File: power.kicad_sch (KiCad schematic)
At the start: 24 parts, among them U1 AP63203WU, U4 XL1509-12, U6 XL1509-12

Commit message: ESC Update with Specifications
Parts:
- C1: value 10uF -> 10u
- C12, C5: value 470uF -> 470u
- C13, C6: value 1uF -> 1u
- C14, C7: value 180uF -> 180u
- C2: value 100nF -> 100n
- C3, C4: value 22uF -> 22u
- D4: value LED -> 3V3Led
- D5: value LED -> FPVLed
- D7: value LED -> 5VLed
- L1: value 4.7uH -> 4.7u
- L2, L4: value 68uH -> 68u
- renumbered U4 to 12V_SD, U1 to 3.3V_SD, U6 to 5V_SD
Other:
- moved on the sheet: D7, R8

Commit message: ESC Update & Finalization Draft
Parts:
- D1: value 1N5820 -> SS34
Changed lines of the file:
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@@
 			)
 		)
-		(property "Value" "1N5820"
+		(property "Value" "SS34"
 			(at 188.214 71.374 90)
 			(effects

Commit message: Less bulky switching regulator for the ESC drivers, PCB update.
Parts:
- 5V_SD1: renamed from 5V_SD; value XL1509-12 -> XL1509-5; footprint Package_SO:SOIC-8_3.9x4.9mm_P1.27mm -> easyeda2kicad:SOIC-8_L5.0-W4.0-P1.27-LS6.0-BL
- D1: footprint Diode_THT:D_DO-201AD_P15.24mm_Horizontal -> easyeda2kicad:SMA_L4.3-W2.6-LS5.2-RD
- D6: value 1N5820 -> SS34; footprint Diode_THT:D_DO-201AD_P15.24mm_Horizontal -> easyeda2kicad:SMA_L4.3-W2.6-LS5.2-RD
- R6: value 100 -> 220
- R7: value 1k -> 5k
- R8: value 270 -> 1k
- renumbered 12V_SD to 12V_SD2, 3.3V_SD to 3.3V_SD1
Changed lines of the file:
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@@
 	)
 	(junction
-		(at 106.68 76.2)
+		(at 95.25 109.22)
 		(diameter 0)
 		(color 0 0 0 0)
 	)
 	(junction
-		(at 95.25 109.22)
+		(at 106.68 76.2)
 		(diameter 0)
 		(color 0 0 0 0)
@@
 	(wire
 		(pts
-			(xy 95.25 109.22) (xy 105.41 109.22)
+			(xy 62.23 78.74) (xy 62.23 73.66)
 		)
 		(stroke
@@
 	(wire
 		(pts
-			(xy 62.23 78.74) (xy 62.23 73.66)
+			(xy 186.69 73.66) (xy 191.77 73.66)
 		)
 		(stroke
@@
 	(wire
 		(pts
-			(xy 186.69 73.66) (xy 191.77 73.66)
+			(xy 92.71 74.93) (xy 92.71 76.2)
 		)
 		(stroke
@@
 	(wire
 		(pts
-			(xy 92.71 74.93) (xy 92.71 76.2)
+			(xy 142.24 81.28) (xy 153.67 81.28)
 		)
 		(stroke
@@
 	(wire
 		(pts
-			(xy 142.24 81.28) (xy 153.67 81.28)
+			(xy 161.29 86.36) (xy 153.67 86.36)
 		)
 		(stroke
@@
 	(wire
 		(pts
-			(xy 161.29 86.36) (xy 153.67 86.36)
+			(xy 95.25 109.22) (xy 105.41 109.22)
 		)
 		(stroke
@@
 			)
 		)
-		(property "Footprint" "Diode_THT:D_DO-201AD_P15.24mm_Horizontal"
+		(property "Footprint" "easyeda2kicad:SMA_L4.3-W2.6-LS5.2-RD"
 			(at 191.135 69.85 0)
 			(effects
@@
 			)
 		)
-		(property "Value" "270"
+		(property "Value" "1k"
 			(at 118.618 116.586 90)
 			(effects
@@
 		(on_board yes)
 		(dnp no)
-		(fields_autoplaced yes)
 		(property "Reference" "D6"
-			(at 97.79 104.4574 90)
+			(at 96.774 104.394 90)
 			(effects
 				(font
@@
 			)
 		)
-		(property "Value" "1N5820"
-			(at 97.79 106.9974 90)
+		(property "Value" "SS34"
+			(at 96.774 106.934 90)
 			(effects
 				(font
@@
 			)
 		)
-		(property "Footprint" "Diode_THT:D_DO-201AD_P15.24mm_Horizontal"
+		(property "Footprint" "easyeda2kicad:SMA_L4.3-W2.6-LS5.2-RD"
 			(at 99.695 105.41 0)
 			(effects
@@
 		)
 		(instances
-			(project ""
+			(project "Drone V3"
 				(path "/6af311bf-2fb1-446c-8c7e-7c930a463809/d145bcf3-ead3-4bb6-b36d-e03e7e63efd9"
 					(reference "D6")
@@
 		(dnp no)
 		(fields_autoplaced yes)
-		(property "Reference" "12V_SD"
+		(property "Reference" "12V_SD2"
 			(at 171.45 66.04 0)
 			(effects
@@
 			(project ""
 				(path "/6af311bf-2fb1-446c-8c7e-7c930a463809/d145bcf3-ead3-4bb6-b36d-e03e7e63efd9"
-					(reference "12V_SD")
+					(reference "12V_SD2")
 					(unit 1)
 				)
@@
 		(dnp no)
 		(fields_autoplaced yes)
-		(property "Reference" "5V_SD"
+		(property "Reference" "5V_SD1"
 			(at 83.82 101.6 0)
 			(effects
@@
 			)
 		)
-		(property "Value" "XL1509-12"
+		(property "Value" "XL1509-5"
 			(at 83.82 104.14 0)
 			(effects
@@
 			)
 		)
-		(property "Footprint" "Package_SO:SOIC-8_3.9x4.9mm_P1.27mm"
+		(property "Footprint" "easyeda2kicad:SOIC-8_L5.0-W4.0-P1.27-LS6.0-BL"
 			(at 83.82 103.378 0)
 			(effects
@@
 			(project ""
 				(path "/6af311bf-2fb1-446c-8c7e-7c930a463809/d145bcf3-ead3-4bb6-b36d-e03e7e63efd9"
-					(reference "5V_SD")
+					(reference "5V_SD1")
 					(unit 1)
 				)
@@
 			)
 		)
-		(property "Value" "100"
+		(property "Value" "220"
 			(at 107.188 86.106 90)
 			(effects
@@
 		(dnp no)
 		(fields_autoplaced yes)
-		(property "Reference" "3.3V_SD"
+		(property "Reference" "3.3V_SD1"
 			(at 76.2 66.04 0)
 			(effects
@@
 			(project ""
 				(path "/6af311bf-2fb1-446c-8c7e-7c930a463809/d145bcf3-ead3-4bb6-b36d-e03e7e63efd9"
-					(reference "3.3V_SD")
+					(reference "3.3V_SD1")
 					(unit 1)
 				)
@@
 			)
 		)
-		(property "Value" "1k"
+		(property "Value" "5k"
 			(at 204.978 83.82 90)
 			(effects

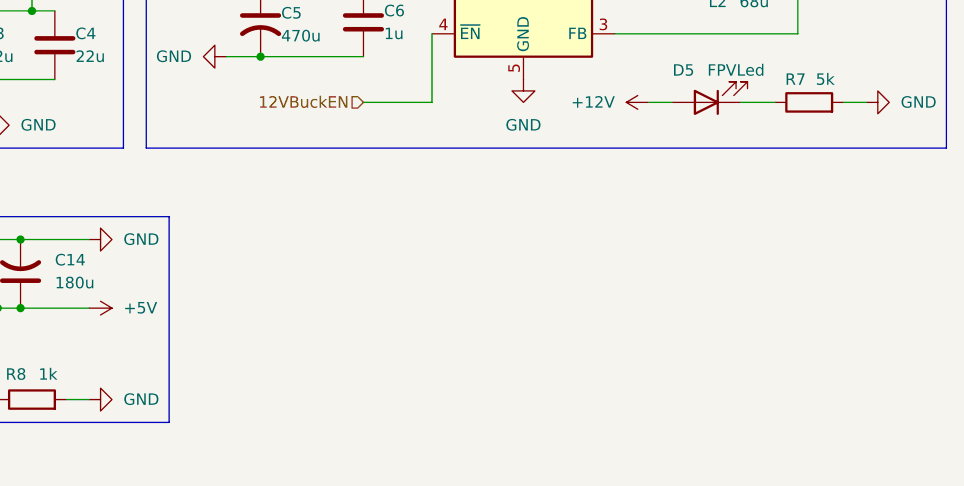
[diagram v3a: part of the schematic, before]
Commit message: MCU implementation start Still needs component schematic checks & component integration with MCU
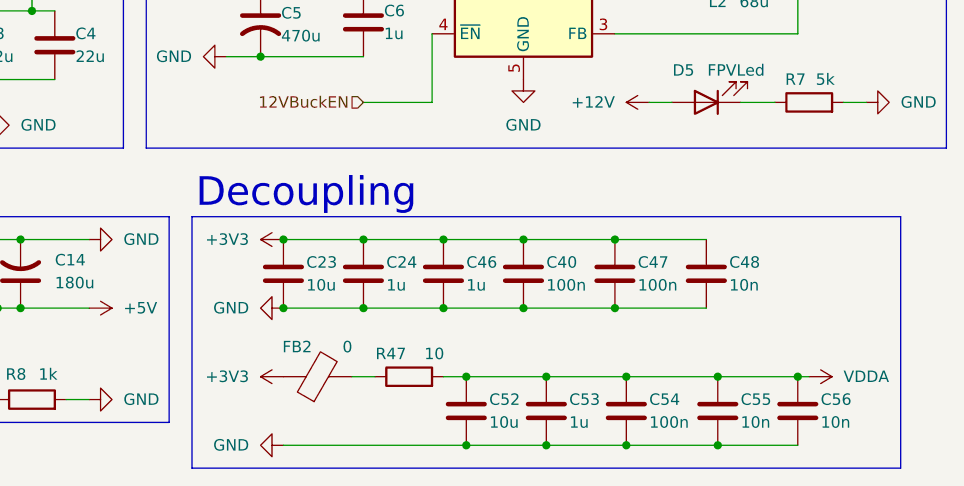
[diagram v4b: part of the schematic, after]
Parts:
- added C23, C52: 10u, symbol Device:C
- added C24, C46, C53: 1u, symbol Device:C
- added C40, C47, C54: 100n, symbol Device:C
- added C48, C55, C56: 10n, symbol Device:C
- added FB2: 0, symbol Device:FerriteBead
- added R47: 10, symbol Device:R
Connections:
- net +3V3: now also C23.1, C24.1, C40.1, C46.1, C47.1, C48.1, FB2.1
- net GND: now also C23.2, C24.2, C40.2, C46.2, C47.2, C48.2, C52.2, C53.2, C54.2, C55.2, C56.2
- new net: FB2.2, R47.1
- new net VDDA: C52.1, C53.1, C54.1, C55.1, C56.1, R47.2
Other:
- note added: "Decoupling"
